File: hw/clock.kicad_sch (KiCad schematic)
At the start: 52 parts, among them J1 USB4105-GF-A, J2 USB-A1HSW6, J3 USB-A1HSW6, SW1 SW_Push, SW2 SW_Push, SW3 SW_Push, U1 LPC812M101JDH20, U10 HDSP-5321 Common Anode, U11 HDSP-5321 Common Anode, U12 HDSP-5321 Common Anode, U13 MCP9808T-E/MS, U14 AP2192ASG-13, U15 INA219AIDR, U16 INA219AIDR, U2 INTERFACE-FT230XS-R_SSOP16_, U3 SN74HC595DR, U4 SN74HC595DR, U5 SN74HC595DR, U6 SN74HC595DR, U7 SN74HC595DR, U8 SN74HC595DR, U9 MCP7940MT-I_SN, Y1 30MHz, Y2 32.768KHz

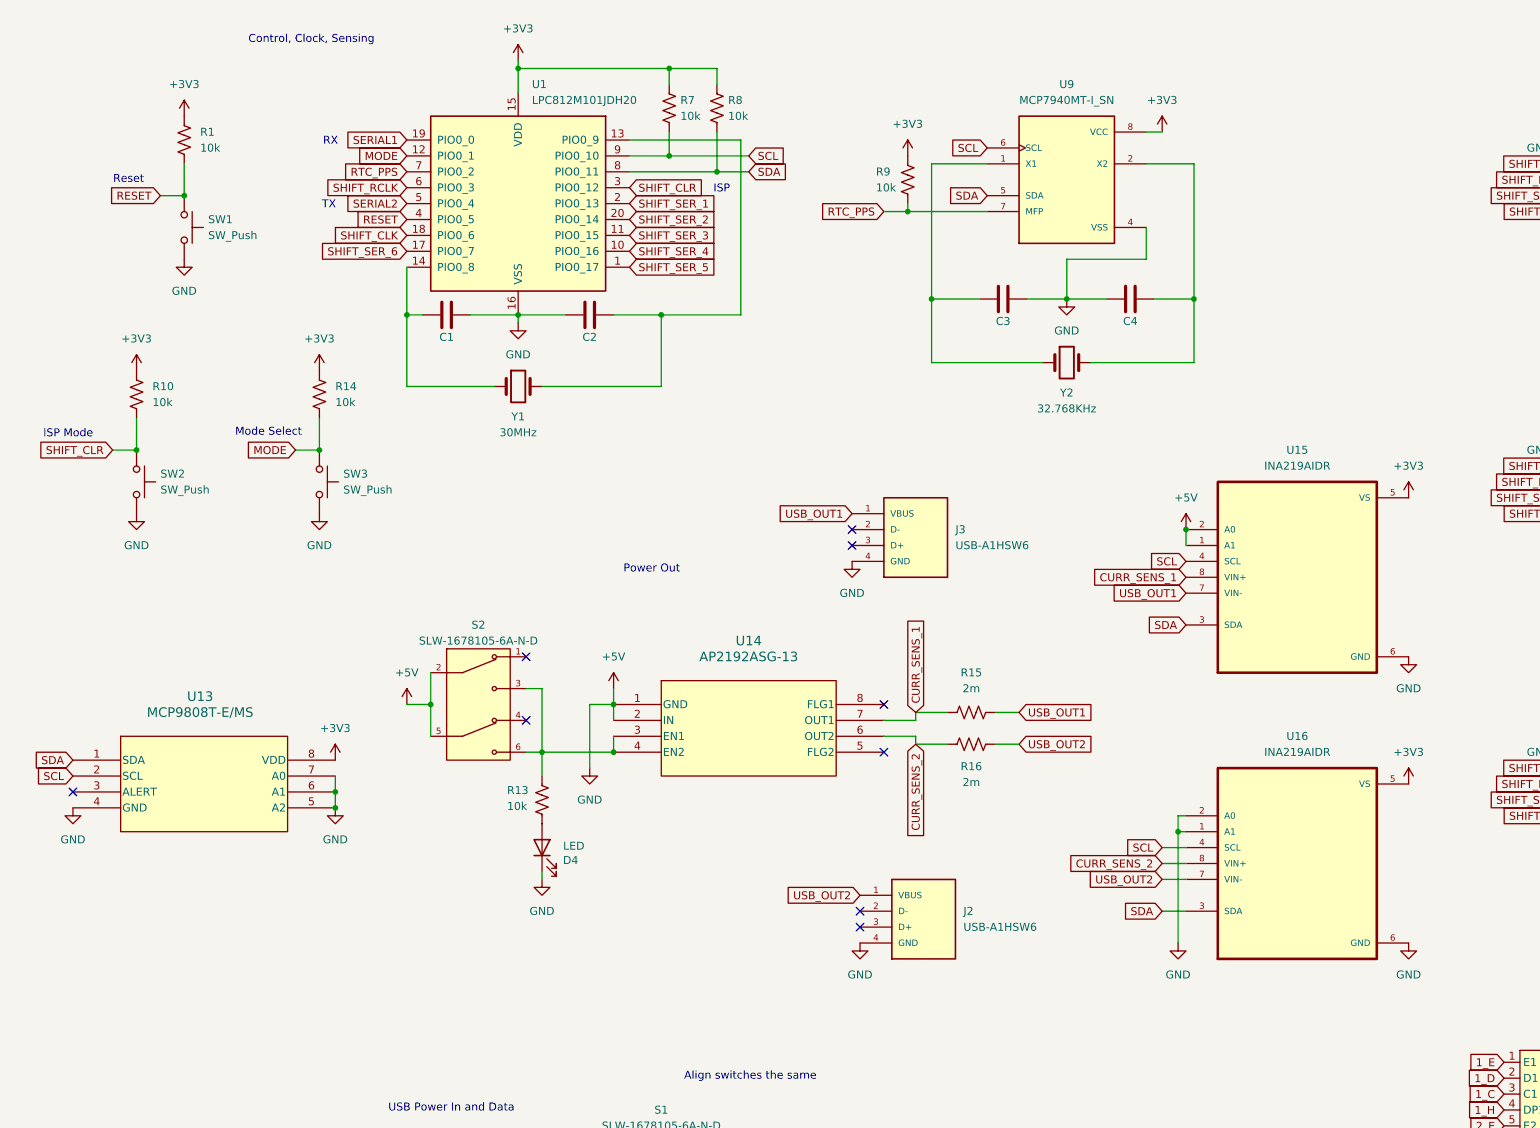
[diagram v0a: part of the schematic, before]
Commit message: Assign footprints
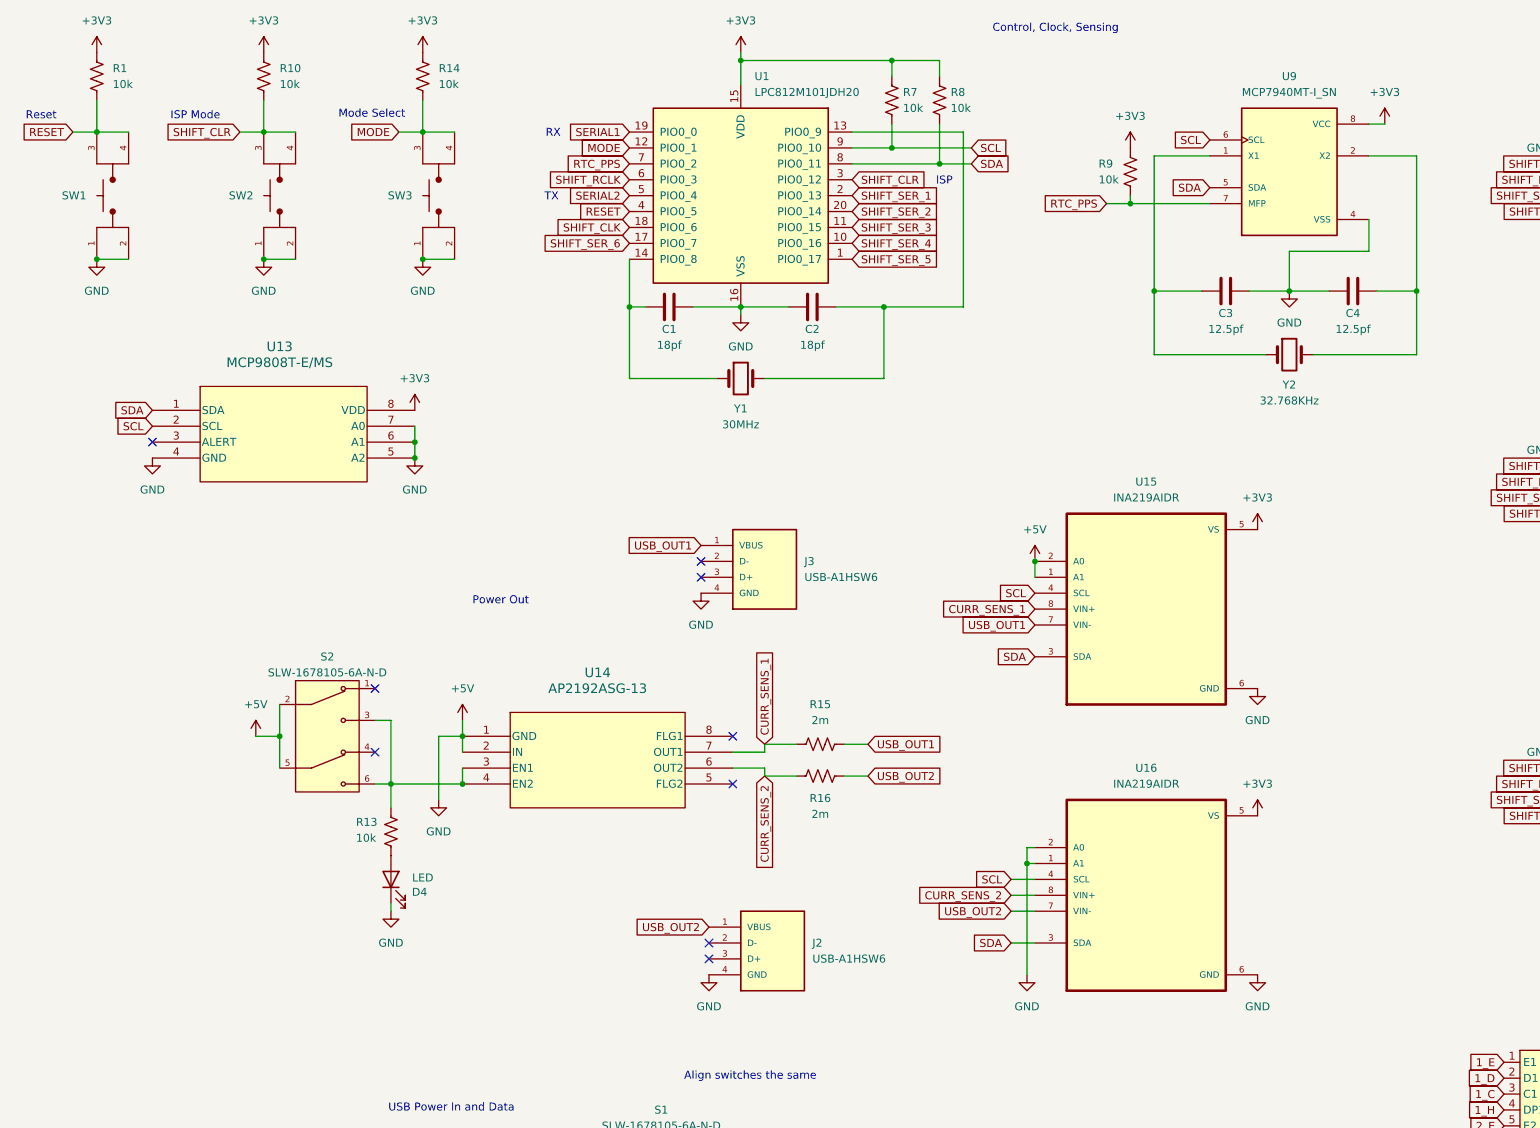
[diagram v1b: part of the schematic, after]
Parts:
- removed SW1, SW2, SW3: SW_Push, symbol Switch:SW_Push
- added SW1, SW2, SW3: TL3305AF260QG, Clock:SW_TL3305AF260QG, symbol TL3305AF260QG:TL3305AF260QG
- C1, C2: value ~ -> 18pf
- C3, C4: value ~ -> 12.5pf
- U10, U11, U12: footprint (none) -> Clock:HDSP-R
- Y1: footprint (none) -> Clock:XTAL_ABLS2-30.000MHZ-D4YF-T
- Y2: footprint (none) -> Clock:XTAL_ECS-.327-12.5-34RR-TR
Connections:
- net +5V: now also SW1.1, SW1.2, SW2.1, SW2.2, SW3.1, SW3.2
- net MODE: now also SW3.3, SW3.4
- net RESET: now also SW1.3, SW1.4
- net SHIFT_CLR: now also SW2.3, SW2.4
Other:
- moved on the sheet: C1, C2, C3, C4, D4, J2, J3, R1, R10, R13, R14, R15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

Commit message: Minor schematic changes, routing
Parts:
- removed J1: USB4105-GF-A, Clock:GCT_USB4105-GF-A, symbol USB4105-GF-A:USB4105-GF-A
- removed R2, R3: 5.1k, Resistor_SMD:R_0805_2012Metric, symbol Device:R_US
- added C10, C6, C7: 1uf, Capacitor_SMD:C_0805_2012Metric, symbol Device:C
- added C8, C9: 120uf, Capacitor_SMD:C_0805_2012Metric, symbol Device:C
- added J1: USB-A1HSW6, Clock:OST_USB-A1HSW6, symbol USB-A1HSW6:USB-A1HSW6
- C5: value 33uf -> 120uf
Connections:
- net +3V3: now also U15.1 (A1), U15.2 (A0)
- net +5V: now also J1.1 (VBUS); no longer C1.2, C2.1, C3.2, C4.1, C5.1, D3.1 (K), D4.1 (K), J2.4 (GND), J3.4 (GND), R12.3, SW1.1, SW1.2, SW2.1, SW2.2, SW3.1, SW3.2, U1.16 (VSS), U13.4 (GND), U13.5 (A2), U13.6 (A1), U13.7 (A0), U14.1 (GND), U15.1 (A1), U15.2 (A0), U15.6 (GND), U16.1 (A1), U16.2 (A0), U16.6 (GND), U2.13 (GND@1), U2.5 (GND), U3.13 (~{OE}), U3.8 (GND), U4.13 (~{OE}), U4.8 (GND), U5.13 (~{OE}), U5.8 (GND), U6.13 (~{OE}), U6.8 (GND), U7.13 (~{OE}), U7.8 (GND), U8.13 (~{OE}), U8.8 (GND), U9.4 (VSS), VR1.2 (GND_2), VR1.4 (GND_4)
- net MODE: now also C10.1
- net USB_OUT1: now also C7.2, C9.2
- net USB_OUT2: now also C6.2, C8.2
- net at S1.3: now also S1.6, VR1.1 (IN)
- net D+: no longer names the net of U2.8 (USBDP)
- net D+: now also J1.3 (D+)
- net D-: no longer names the net of U2.9 (USBDM)
- net D-: now also J1.2 (D-)
- new net GND: C1.2, C10.2, C2.1, C3.2, C4.1, C5.1, C6.1, C7.1, C8.1, C9.1, D3.1 (K), D4.1 (K), J1.4 (GND), J2.4 (GND), J3.4 (GND), R12.3, SW1.1, SW1.2, SW2.1, SW2.2, SW3.1, SW3.2, U1.16 (VSS), U13.4 (GND), U13.5 (A2), U13.6 (A1), U13.7 (A0), U14.1 (GND), U15.6 (GND), U16.1 (A1), U16.2 (A0), U16.6 (GND), U2.13 (GND@1), U2.5 (GND), U3.13 (~{OE}), U3.8 (GND), U4.13 (~{OE}), U4.8 (GND), U5.13 (~{OE}), U5.8 (GND), U6.13 (~{OE}), U6.8 (GND), U7.13 (~{OE}), U7.8 (GND), U8.13 (~{OE}), U8.8 (GND), U9.4 (VSS), VR1.2 (GND_2), VR1.4 (GND_4)
- now unconnected: S1.1, S1.4
- no-connect marks 22 -> 20
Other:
- note added: "Serial lines used for programming + syncing"
- note removed: "Align switches the same"
- note removed: "Serial lines used for programming, control"
- moved on the sheet: C5, D1, D2, D4, J2, J3, R1, R10, R13, R14, R15, R16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

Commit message: Routing and minor schematic changes
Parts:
- R13: value 10k -> 15k
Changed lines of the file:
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@@
 			)
 		)
-		(property "Value" "10k"
+		(property "Value" "15k"
 			(at 50.292 147.066 0)
 			(effects

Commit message: Update hw
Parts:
- added C11, C12: 47pf, Capacitor_SMD:C_0805_2012Metric, symbol Device:C
- added C13: 10nf, Capacitor_SMD:C_0805_2012Metric, symbol Device:C
- added R2, R3: 27, Resistor_SMD:R_0805_2012Metric, symbol Device:R_US
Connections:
- net +5V: now also C13.2
- net GND: now also C11.1, C12.1, C13.1
- net at J1.3 (D+): now also C12.2, R2.1; no longer U2.8 (USBDP)
- net at U2.9 (USBDM): now also R3.1; no longer J1.2 (D-)
- new net: R2.2, U2.8 (USBDP)
- new net: C11.2, J1.2 (D-), R3.2
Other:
- note added: "7/5/25"
- note added: "USB Hub Clock"
- note removed: "6/8/25"
- note removed: "High Precision Clock"
- moved on the sheet: J1

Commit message: Final touches
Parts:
- added R17, R18: 0, Resistor_SMD:R_0805_2012Metric, symbol Device:R_US
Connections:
- net at J2.2 (D-): now also R17.2
- net at J2.3 (D+): now also R17.1
- net at J3.2 (D-): now also R18.2
- net at J3.3 (D+): now also R18.1
- no-connect marks 20 -> 16
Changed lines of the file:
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@@
 	)
 	(no_connect
-		(at 128.27 168.91)
-	)
-	(no_connect
 		(at 53.34 123.19)
 	)
@@
 	)
 	(no_connect
-		(at 128.27 171.45)
-	)
-	(no_connect
 		(at 110.49 130.81)
 	)
@@
 	)
 	(no_connect
-		(at 128.27 96.52)
-	)
-	(no_connect
-		(at 128.27 99.06)
-	)
-	(no_connect
 		(at 110.49 138.43)
 	)
@@
 	(wire
 		(pts
+			(xy 116.84 168.91) (xy 128.27 168.91)
+		)
+		(stroke
+			(width 0)
+			(type default)
+		)
+	)
+	(wire
+		(pts
 			(xy 177.8 157.48) (xy 181.61 157.48)
 		)
@@
 	(wire
 		(pts
+			(xy 125.73 99.06) (xy 128.27 99.06)
+		)
+		(stroke
+			(width 0)
+			(type default)
+		)
+	)
+	(wire
+		(pts
 			(xy 81.28 252.73) (xy 81.28 234.95)
 		)
@@
 	(wire
 		(pts
+			(xy 116.84 96.52) (xy 128.27 96.52)
+		)
+		(stroke
+			(width 0)
+			(type default)
+		)
+	)
+	(wire
+		(pts
 			(xy 55.88 55.88) (xy 60.96 55.88)
 		)
@@
 	(wire
 		(pts
+			(xy 116.84 99.06) (xy 118.11 99.06)
+		)
+		(stroke
+			(width 0)
+			(type default)
+		)
+	)
+	(wire
+		(pts
 			(xy 125.73 264.16) (xy 158.75 264.16)
 		)
@@
 	(wire
 		(pts
+			(xy 116.84 171.45) (xy 118.11 171.45)
+		)
+		(stroke
+			(width 0)
+			(type default)
+		)
+	)
+	(wire
+		(pts
 			(xy 80.01 217.17) (xy 80.01 214.63)
 		)
@@
 	(wire
 		(pts
+			(xy 116.84 171.45) (xy 116.84 168.91)
+		)
+		(stroke
+			(width 0)
+			(type default)
+		)
+	)
+	(wire
+		(pts
 			(xy 74.93 213.36) (xy 74.93 214.63)
 		)
@@
 	(wire
 		(pts
+			(xy 125.73 171.45) (xy 128.27 171.45)
+		)
+		(stroke
+			(width 0)
+			(type default)
+		)
+	)
+	(wire
+		(pts
 			(xy 146.05 219.71) (xy 153.67 219.71)
 		)
@@
 	(wire
 		(pts
+			(xy 116.84 99.06) (xy 116.84 96.52)
+		)
+		(stroke
+			(width 0)
+			(type default)
+		)
+	)
+	(wire
+		(pts
 			(xy 144.78 137.16) (xy 144.78 139.7)
 		)
@@
 	)
 	(symbol
+		(lib_id "Device:R_US")
+		(at 121.92 171.45 270)
+		(unit 1)
+		(exclude_from_sim no)
+		(in_bom yes)
+		(on_board yes)
+		(dnp no)
+		(property "Reference" "R17"
+			(at 121.92 174.244 90)
+			(effects
+				(font
+					(size 1.27 1.27)
+				)
+			)
+		)
+		(property "Value" "0"
+			(at 121.92 176.784 90)
+			(effects
+				(font
+					(size 1.27 1.27)
+				)
+			)
+		)
+		(property "Footprint" "Resistor_SMD:R_0805_2012Metric"
+			(at 121.666 172.466 90)
+			(effects
+				(font
+					(size 1.27 1.27)
+				)
+				(hide yes)
+			)
+		)
+		(property "Datasheet" "~"
+			(at 121.92 171.45 0)
+			(effects
+				(font
+					(size 1.27 1.27)
+				)
+				(hide yes)
+			)
+		)
+		(property "Description" "Resistor, US symbol"
+			(at 121.92 171.45 0)
+			(effects
+				(font
+					(size 1.27 1.27)
+				)
+				(hide yes)
+			)
+		)
+		(pin "1"
+		)
+		(pin "2"
+		)
+		(instances
+			(project "clock"
+				(path "/28b01b40-bc27-47b8-871a-e15e2a104d00"
+					(reference "R17")
+					(unit 1)
+				)
+			)
+		)
+	)
+	(symbol
 		(lib_id "power:GND")
 		(at 267.97 86.36 270)
@@
 					(unit 1)
 				)
+			)
+		)
+	)
+	(symbol
+		(lib_id "Device:R_US")
+		(at 121.92 99.06 270)
+		(unit 1)
+		(exclude_from_sim no)
+		(in_bom yes)
+		(on_board yes)
+		(dnp no)
+		(property "Reference" "R18"
+			(at 121.92 101.854 90)
+			(effects
+				(font
+					(size 1.27 1.27)
+				)
+			)
+		)
+		(property "Value" "0"
+			(at 121.92 104.394 90)
+			(effects
+				(font
+					(size 1.27 1.27)
+				)
+			)
+		)
+		(property "Footprint" "Resistor_SMD:R_0805_2012Metric"
+			(at 121.666 100.076 90)
+			(effects
+				(font
+					(size 1.27 1.27)
+				)
+				(hide yes)
+			)
+		)
+		(property "Datasheet" "~"
+			(at 121.92 99.06 0)
+			(effects
+				(font
+					(size 1.27 1.27)
+				)
+				(hide yes)
+			)
+		)
+		(property "Description" "Resistor, US symbol"
+			(at 121.92 99.06 0)
+			(effects
+				(font
+					(size 1.27 1.27)
+				)
+				(hide yes)
+			)
+		)
+		(pin "1"
+		)
+		(pin "2"
+		)
+		(instances
+			(project "clock"
+				(path "/28b01b40-bc27-47b8-871a-e15e2a104d00"
+					(reference "R18")
+					(unit 1)
+				)

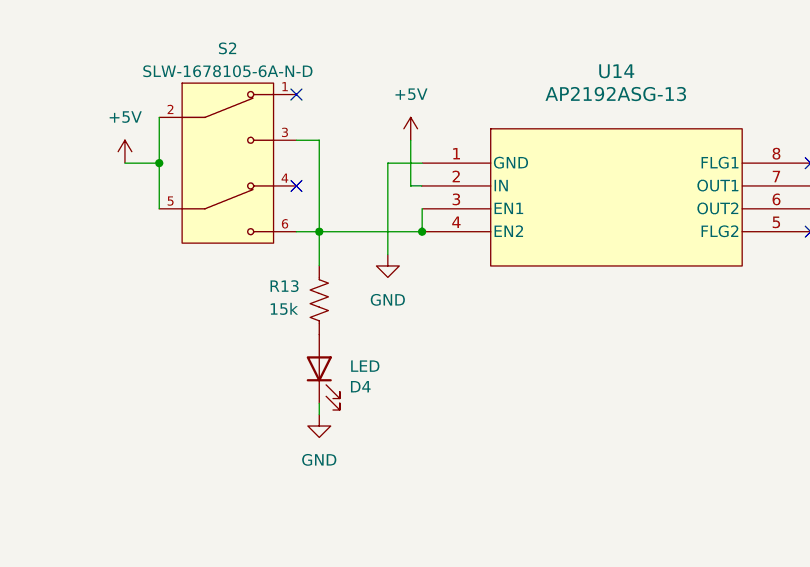
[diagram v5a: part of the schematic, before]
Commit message: Add pull load switch pull down
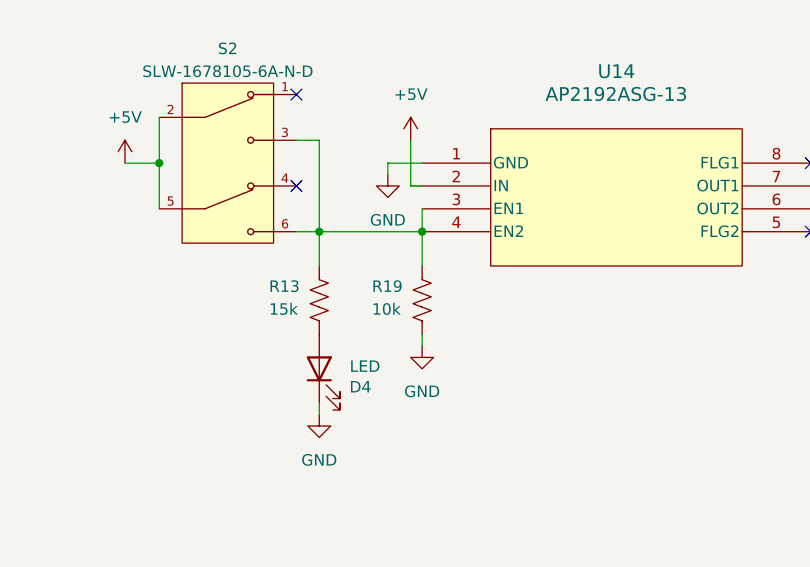
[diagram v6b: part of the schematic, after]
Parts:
- added R19: 10k, Resistor_SMD:R_0805_2012Metric, symbol Device:R_US
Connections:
- net GND: now also R19.1
- net at R13.2, S2.3, S2.6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: now also R19.2
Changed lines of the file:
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@@
 	(paper "A3")
 	(junction
-		(at 55.88 138.43)
-		(diameter 0)
-		(color 0 0 0 0)
-	)
-	(junction
 		(at 87.63 214.63)
 		(diameter 0)
@@
 	)
 	(junction
+		(at 55.88 138.43)
+		(diameter 0)
+		(color 0 0 0 0)
+	)
+	(junction
 		(at 158.75 38.1)
 		(diameter 0)
@@
 	(wire
 		(pts
-			(xy 55.88 138.43) (xy 67.31 138.43)
-		)
-		(stroke
-			(width 0)
-			(type default)
-		)
-	)
-	(wire
-		(pts
 			(xy 158.75 24.13) (xy 166.37 24.13)
 		)
@@
 	(wire
 		(pts
-			(xy 63.5 140.97) (xy 63.5 130.81)
+			(xy 63.5 132.08) (xy 63.5 130.81)
 		)
 		(stroke
@@
 	(wire
 		(pts
-			(xy 55.88 138.43) (xy 55.88 142.24)
-		)
-		(stroke
-			(width 0)
-			(type default)
-		)
-	)
-	(wire
-		(pts
 			(xy 127 63.5) (xy 134.62 63.5)
 		)
@@
 	(wire
 		(pts
+			(xy 55.88 138.43) (xy 55.88 142.24)
+		)
+		(stroke
+			(width 0)
+			(type default)
+		)
+	)
+	(wire
+		(pts
 			(xy 81.28 234.95) (xy 66.04 234.95)
 		)
@@
 	(wire
 		(pts
+			(xy 67.31 149.86) (xy 67.31 151.13)
+		)
+		(stroke
+			(width 0)
+			(type default)
+		)
+	)
+	(wire
+		(pts
 			(xy 248.92 259.08) (xy 248.92 255.27)
 		)
@@
 	(wire
 		(pts
+			(xy 67.31 138.43) (xy 67.31 142.24)
+		)
+		(stroke
+			(width 0)
+			(type default)
+		)
+	)
+	(wire
+		(pts
 			(xy 248.92 236.22) (xy 248.92 240.03)
 		)
@@
 	(wire
 		(pts
+			(xy 55.88 138.43) (xy 67.31 138.43)
+		)
+		(stroke
+			(width 0)
+			(type default)
+		)
+	)
+	(wire
+		(pts
 			(xy 55.88 35.56) (xy 60.96 35.56)
 		)
@@
 	(symbol
 		(lib_id "power:GND")
-		(at 63.5 140.97 0)
+		(at 67.31 151.13 0)
+		(unit 1)
+		(exclude_from_sim no)
+		(in_bom yes)
+		(on_board yes)
+		(dnp no)
+		(fields_autoplaced yes)
+		(property "Reference" "#PWR063"
+			(at 67.31 157.48 0)
+			(effects
+				(font
+					(size 1.27 1.27)
+				)
+				(hide yes)
+			)
+		)
+		(property "Value" "GND"
+			(at 67.31 156.21 0)
+			(effects
+				(font
+					(size 1.27 1.27)
+				)
+			)
+		)
+		(property "Footprint" ""
+			(at 67.31 151.13 0)
+			(effects
+				(font
+					(size 1.27 1.27)
+				)
+				(hide yes)
+			)
+		)
+		(property "Datasheet" ""
+			(at 67.31 151.13 0)
+			(effects
+				(font
+					(size 1.27 1.27)
+				)
+				(hide yes)
+			)
+		)
+		(property "Description" "Power symbol creates a global label with name \"GND\" , ground"
+			(at 67.31 151.13 0)
+			(effects
+				(font
+					(size 1.27 1.27)
+				)
+				(hide yes)
+			)
+		)
+		(pin "1"
+		)
+		(instances
+			(project "clock"
+				(path "/28b01b40-bc27-47b8-871a-e15e2a104d00"
+					(reference "#PWR063")
+					(unit 1)
+				)
+			)
+		)
+	)
+	(symbol
+		(lib_id "power:GND")
+		(at 63.5 132.08 0)
 		(unit 1)
 		(exclude_from_sim no)
@@
 		(fields_autoplaced yes)
 		(property "Reference" "#PWR049"
-			(at 63.5 147.32 0)
+			(at 63.5 138.43 0)
 			(effects
 				(font
@@
 		)
 		(property "Value" "GND"
-			(at 63.5 146.05 0)
+			(at 63.5 137.16 0)
 			(effects
 				(font
@@
 		)
 		(property "Footprint" ""
-			(at 63.5 140.97 0)
+			(at 63.5 132.08 0)
 			(effects
 				(font
@@
 		)
 		(property "Datasheet" ""
-			(at 63.5 140.97 0)
+			(at 63.5 132.08 0)
 			(effects
 				(font
@@
 		)
 		(property "Description" "Power symbol creates a global label with name \"GND\" , ground"
-			(at 63.5 140.97 0)
+			(at 63.5 132.08 0)
 			(effects
 				(font
@@
 					(unit 1)
 				)
+			)
+		)
+	)
+	(symbol
+		(lib_id "Device:R_US")
+		(at 67.31 146.05 180)
+		(unit 1)
+		(exclude_from_sim no)
+		(in_bom yes)
+		(on_board yes)
+		(dnp no)
+		(property "Reference" "R19"
+			(at 61.722 144.526 0)
+			(effects
+				(font
+					(size 1.27 1.27)
+				)
+				(justify right)
+			)
+		)
+		(property "Value" "10k"
+			(at 61.722 147.066 0)
+			(effects
+				(font
+					(size 1.27 1.27)
+				)
+				(justify right)
+			)
+		)
+		(property "Footprint" "Resistor_SMD:R_0805_2012Metric"
+			(at 66.294 145.796 90)
+			(effects
+				(font
+					(size 1.27 1.27)
+				)
+				(hide yes)
+			)
+		)
+		(property "Datasheet" "~"
+			(at 67.31 146.05 0)
+			(effects
+				(font
+					(size 1.27 1.27)
+				)
+				(hide yes)
+			)
+		)
+		(property "Description" "Resistor, US symbol"
+			(at 67.31 146.05 0)
+			(effects
+				(font
+					(size 1.27 1.27)
+				)
+				(hide yes)
+			)
+		)
+		(pin "1"
+		)
+		(pin "2"
+		)
+		(instances
+			(project "clock"
+				(path "/28b01b40-bc27-47b8-871a-e15e2a104d00"
+					(reference "R19")
+					(unit 1)
+				)
